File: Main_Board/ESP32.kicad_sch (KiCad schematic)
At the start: 24 parts, among them J1 RESET, J2 MAIN_UART, Q1 2N7002, U1 W25Q128JVS, U2 ESP32-S3-MINI-1U

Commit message: sch update
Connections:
- net CLK_SPI2: now also U2.17 (IO13); no longer U2.18 (IO14)
- net IO0 / MOSI: now also U2.18 (IO14); no longer U2.17 (IO13)
- net IO2 / WP: now also U2.19 (IO15); no longer U2.16 (IO12)
- net IO3 / HOLD: now also U2.16 (IO12); no longer U2.19 (IO15)
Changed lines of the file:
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@@
+	(wire
+		(pts
+			(xy 97.79 110.49) (xy 57.15 110.49)
+		)
+		(stroke
+			(width 0)
+			(type default)
+		)
+	)
+	(wire
+		(pts
+			(xy 104.14 107.95) (xy 104.14 110.49)
+		)
+		(stroke
+			(width 0)
+			(type default)
+		)
+	)
+	(wire
+		(pts
+			(xy 97.79 102.87) (xy 97.79 110.49)
+		)
+		(stroke
+			(width 0)
+			(type default)
+		)
+	)
 	(wire
 		(pts
@@
 	(wire
 		(pts
-			(xy 107.95 100.33) (xy 107.95 107.95)
+			(xy 107.95 100.33) (xy 107.95 105.41)
 		)
 		(stroke
@@
 	(wire
 		(pts
+			(xy 115.57 102.87) (xy 97.79 102.87)
+		)
+		(stroke
+			(width 0)
+			(type default)
+		)
+	)
+	(wire
+		(pts
 			(xy 36.83 36.83) (xy 36.83 55.88)
 		)
@@
 	(wire
 		(pts
-			(xy 115.57 105.41) (xy 92.71 105.41)
-		)
-		(stroke
-			(width 0)
-			(type default)
-		)
-	)
-	(wire
-		(pts
 			(xy 190.5 57.15) (xy 191.77 57.15)
 		)
@@
 	(wire
 		(pts
+			(xy 105.41 107.95) (xy 105.41 105.41)
+		)
+		(stroke
+			(width 0)
+			(type default)
+		)
+	)
+	(wire
+		(pts
 			(xy 104.14 67.31) (xy 115.57 67.31)
 		)
@@
 	(wire
 		(pts
+			(xy 105.41 105.41) (xy 92.71 105.41)
+		)
+		(stroke
+			(width 0)
+			(type default)
+		)
+	)
+	(wire
+		(pts
 			(xy 160.02 110.49) (xy 146.05 110.49)
 		)
@@
 	(wire
 		(pts
-			(xy 104.14 102.87) (xy 104.14 107.95)
+			(xy 104.14 110.49) (xy 115.57 110.49)
 		)
 		(stroke
@@
 	(wire
 		(pts
-			(xy 115.57 107.95) (xy 107.95 107.95)
+			(xy 115.57 105.41) (xy 107.95 105.41)
 		)
 		(stroke
@@
 	(wire
 		(pts
-			(xy 115.57 102.87) (xy 104.14 102.87)
-		)
-		(stroke
-			(width 0)
-			(type default)
-		)
-	)
-	(wire
-		(pts
 			(xy 21.59 60.96) (xy 25.4 60.96)
 		)
@@
 	(wire
 		(pts
+			(xy 115.57 107.95) (xy 105.41 107.95)
+		)
+		(stroke
+			(width 0)
+			(type default)
+		)
+	)
+	(wire
+		(pts
 			(xy 229.87 64.77) (xy 223.52 64.77)
 		)
@@
 		)
 		(stroke
-			(width 0)
-			(type default)
-		)
-	)
-	(wire
-		(pts
-			(xy 57.15 110.49) (xy 115.57 110.49)
-		)
-		(stroke

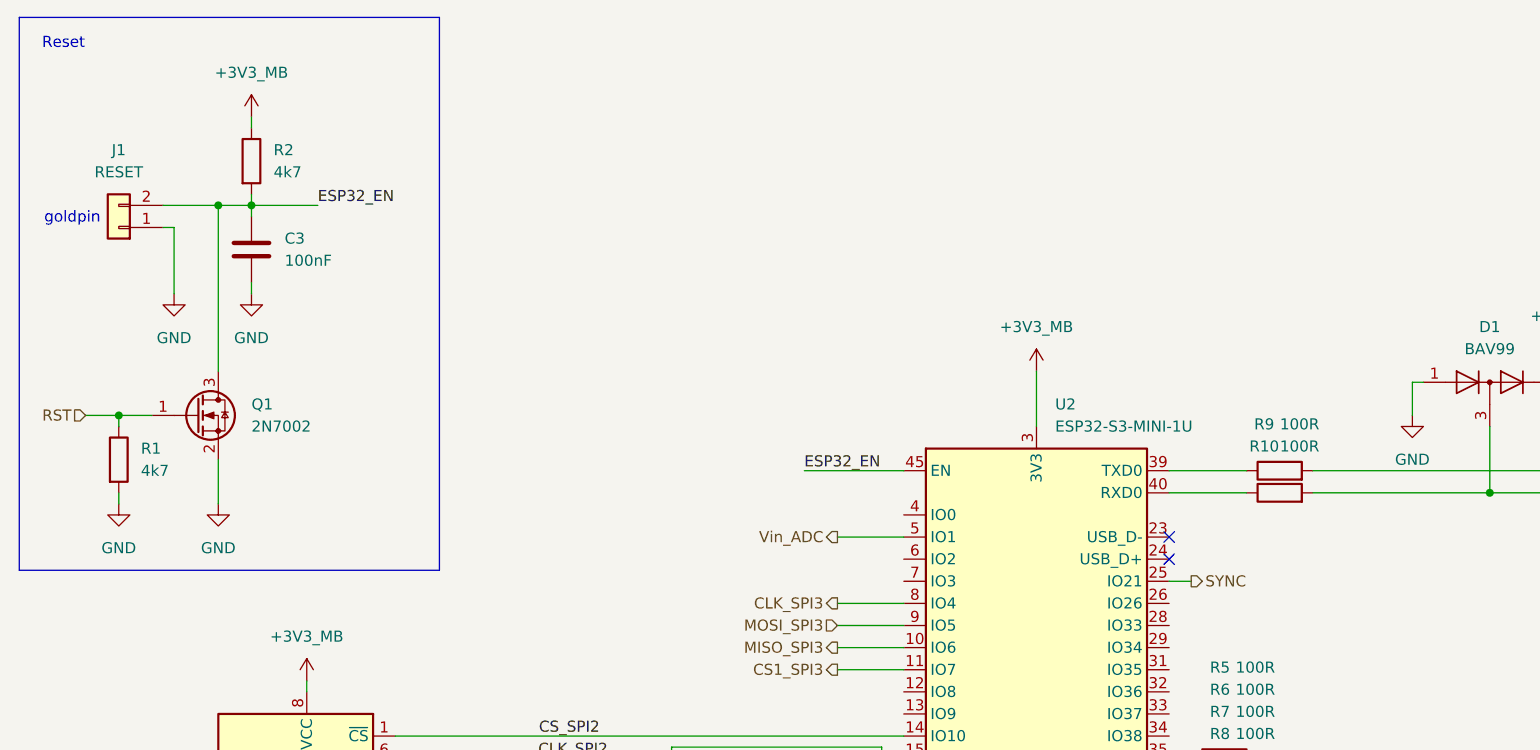
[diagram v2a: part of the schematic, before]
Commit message: Module bus fix
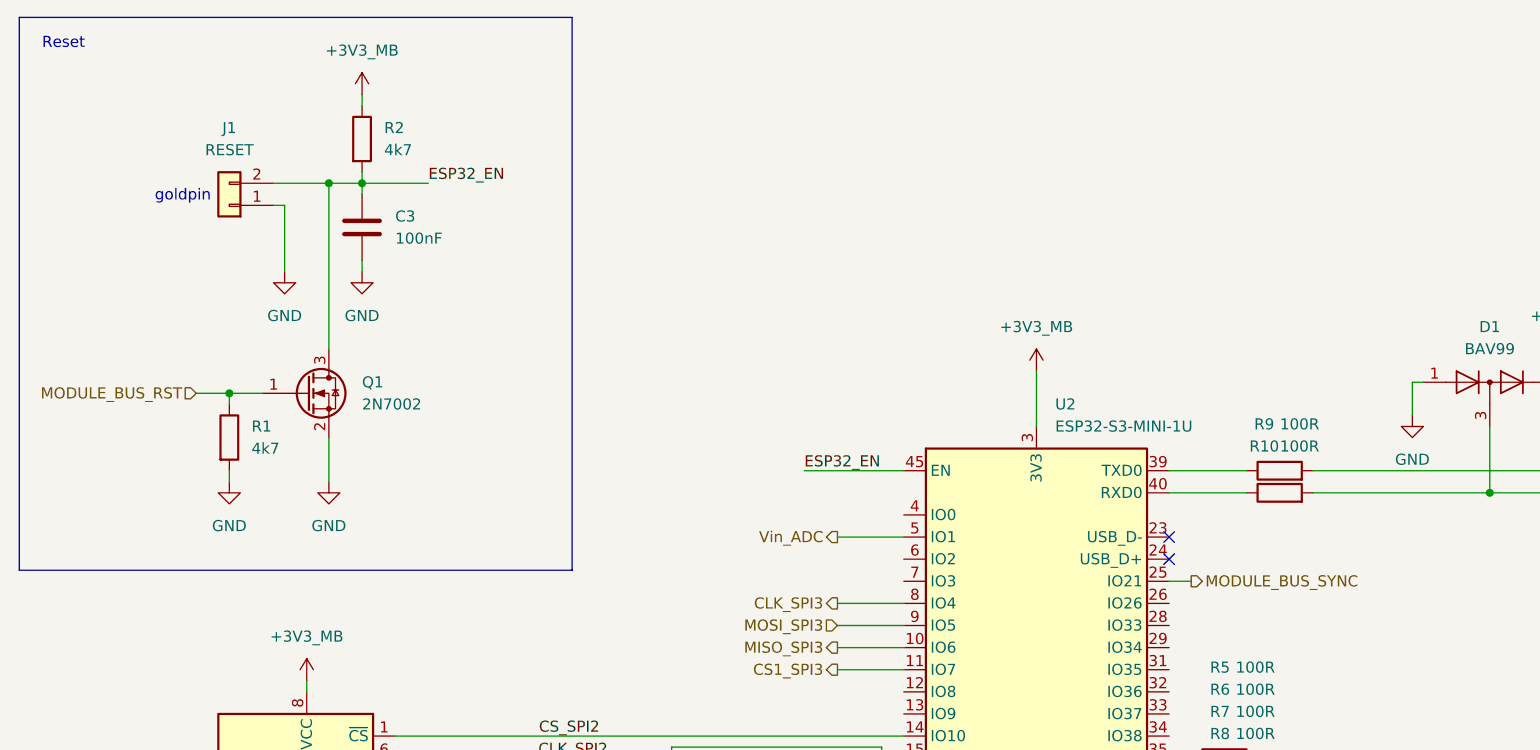
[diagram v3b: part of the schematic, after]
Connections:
- net RST renamed MODULE_BUS_RST
- net SYNC renamed MODULE_BUS_SYNC
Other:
- moved on the sheet: C3, J1, Q1, R1, R2

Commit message: Update main sheet for pyros
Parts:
- added R40, R41: 100R, Resistor_SMD:R_0603_1608Metric, symbol Device:R
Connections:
- net at U2.33 (IO37): now also R40.1
- net at U2.34 (IO38): now also R41.1
- net Piro1 renamed PYRO1
- net Piro2 renamed PYRO2
- new net PYRO1_CONTINUITY: R40.2
- new net PYRO2_CONTINUITY: R41.2

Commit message: Fix schematic readibility
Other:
- moved on the sheet: C3, D1, D2, J1, J2, Q1, R1, R10, R11, R2, R3, R4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

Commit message: Change connector footprints
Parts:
- J2: footprint Connector_PinHeader_2.54mm:PinHeader_1x04_P2.54mm_Horizontal -> Connector_PinHeader_2.54mm:PinHeader_1x04_P2.54mm_Vertical
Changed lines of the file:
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@@
 			)
 		)
-		(property "Footprint" "Connector_PinHeader_2.54mm:PinHeader_1x04_P2.54mm_Horizontal"
+		(property "Footprint" "Connector_PinHeader_2.54mm:PinHeader_1x04_P2.54mm_Vertical"
 			(at 252.73 99.06 0)
 			(hide yes)

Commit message: Remove buzzer circuitry
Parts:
- removed R6: 100R, Resistor_SMD:R_0603_1608Metric, symbol Device:R
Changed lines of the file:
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@@
-	(wire
-		(pts
-			(xy 156.21 134.62) (xy 158.75 134.62)
-		)
-		(stroke
-			(width 0)
-			(type default)
-		)
-	)
 	(wire
 		(pts
@@
 		(pts
 			(xy 245.11 96.52) (xy 247.65 96.52)
-		)
-		(stroke
-			(width 0)
-			(type default)
-		)
-	)
-	(wire
-		(pts
-			(xy 170.18 134.62) (xy 166.37 134.62)
 		)
 		(stroke
@@
 			)
 			(justify left bottom)
-		)
-	)
-	(hierarchical_label "BUZZER"
-		(shape output)
-		(at 170.18 134.62 0)
-		(effects
-			(font
-				(size 1.27 1.27)
-			)
-			(justify left)
 		)
 	)
@@
 					(unit 1)
 				)
-			)
-		)
-	)
-	(symbol
-		(lib_id "Device:R")
-		(at 162.56 134.62 90)
-		(unit 1)
-		(body_style 1)
-		(exclude_from_sim no)
-		(in_bom yes)
-		(on_board yes)
-		(in_pos_files yes)
-		(dnp no)
-		(property "Reference" "R6"
-			(at 181.61 134.62 90)
-			(show_name no)
-			(do_not_autoplace no)
-			(effects
-				(font
-					(size 1.27 1.27)
-				)
-			)
-		)
-		(property "Value" "100R"
-			(at 185.674 134.62 90)
-			(show_name no)
-			(do_not_autoplace no)
-			(effects
-				(font
-					(size 1.27 1.27)
-				)
-			)
-		)
-		(property "Footprint" "Resistor_SMD:R_0603_1608Metric"
-			(at 162.56 136.398 90)
-			(hide yes)
-			(show_name no)
-			(do_not_autoplace no)
-			(effects
-				(font
-					(size 1.27 1.27)
-				)
-			)
-		)
-		(property "Datasheet" ""
-			(at 162.56 134.62 0)
-			(hide yes)
-			(show_name no)
-			(do_not_autoplace no)
-			(effects
-				(font
-					(size 1.27 1.27)
-				)
-			)
-		)
-		(property "Description" "Resistor"
-			(at 162.56 134.62 0)
-			(hide yes)
-			(show_name no)
-			(do_not_autoplace no)
-			(effects
-				(font
-					(size 1.27 1.27)
-				)
-			)
-		)
-		(pin "1"
-		)
-		(pin "2"
-		)
-		(instances
-			(project "Main_Board"
-				(path "/7481738f-7c20-40bb-99b0-6ccd4168db33/cbc83c60-d43e-479b-a6b3-ba8e24d176e0"
-					(reference "R6")
-					(unit 1)
-				)

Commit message: layout update
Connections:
- net CLK_SPI3 is gone; now on an unnamed net: U2.8 (IO4)
- net CS1_SPI3 is gone; now on an unnamed net: U2.11 (IO7)
- net MISO_SPI3 is gone; now on an unnamed net: U2.10 (IO6)
- net MOSI_SPI3 is gone; now on an unnamed net: U2.9 (IO5)
- net at R41.1: no longer U2.34 (IO38)
- net at R40.1: no longer U2.33 (IO37)
- net at R7.1: no longer U2.37 (IO41)
- net at R8.1: no longer U2.38 (IO42)
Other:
- moved on the sheet: R40, R41, R7, R8
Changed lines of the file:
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@@
 	(wire
 		(pts
-			(xy 156.21 129.54) (xy 158.75 129.54)
-		)
-		(stroke
-			(width 0)
-			(type default)
-		)
-	)
-	(wire
-		(pts
 			(xy 233.68 96.52) (xy 233.68 86.36)
 		)
@@
 	(wire
 		(pts
-			(xy 170.18 129.54) (xy 166.37 129.54)
+			(xy 106.68 116.84) (xy 110.49 116.84)
 		)
 		(stroke
@@
 	(wire
 		(pts
-			(xy 170.18 127) (xy 166.37 127)
+			(xy 106.68 114.3) (xy 110.49 114.3)
 		)
 		(stroke
@@
 	(wire
 		(pts
-			(xy 170.18 139.7) (xy 166.37 139.7)
+			(xy 106.68 121.92) (xy 110.49 121.92)
 		)
 		(stroke
@@
 	(wire
 		(pts
-			(xy 170.18 137.16) (xy 166.37 137.16)
+			(xy 106.68 119.38) (xy 110.49 119.38)
 		)
 		(stroke
@@
 	(wire
 		(pts
-			(xy 156.21 127) (xy 158.75 127)
-		)
-		(stroke
-			(width 0)
-			(type default)
-		)
-	)
-	(wire
-		(pts
 			(xy 140.97 87.63) (xy 140.97 93.98)
 		)
@@
 		)
 	)
-	(hierarchical_label "CLK_SPI3"
-		(shape output)
-		(at 118.11 114.3 180)
-		(effects
-			(font
-				(size 1.27 1.27)
-			)
-			(justify right)
-		)
-	)
 	(hierarchical_label "5V_PG"
 		(shape output)
@@
 	(hierarchical_label "PYRO2_CONTINUITY"
 		(shape input)
-		(at 170.18 129.54 0)
-		(effects
-			(font
-				(size 1.27 1.27)
-			)
-			(justify left)
-		)
-	)
-	(hierarchical_label "MISO_SPI3"
-		(shape output)
-		(at 118.11 119.38 180)
+		(at 106.68 116.84 180)
 		(effects
 			(font
@@
 	(hierarchical_label "PYRO1_CONTINUITY"
 		(shape input)
-		(at 170.18 127 0)
+		(at 106.68 114.3 180)
 		(effects
 			(font
 				(size 1.27 1.27)
 			)
-			(justify left)
+			(justify right)
 		)
 	)
 	(hierarchical_label "PYRO1"
 		(shape output)
-		(at 170.18 137.16 0)
-		(effects
-			(font
-				(size 1.27 1.27)
-			)
-			(justify left)
-		)
-	)
-	(hierarchical_label "CS1_SPI3"
-		(shape output)
-		(at 118.11 121.92 180)
+		(at 106.68 119.38 180)
 		(effects
 			(font
@@
 	(hierarchical_label "PYRO2"
 		(shape output)
-		(at 170.18 139.7 0)
+		(at 106.68 121.92 180)
 		(effects
 			(font
 				(size 1.27 1.27)
 			)
-			(justify left)
+			(justify right)
 		)
 	)
@@
 		)
 	)
-	(hierarchical_label "MOSI_SPI3"
-		(shape input)
-		(at 118.11 116.84 180)
-		(effects
-			(font
-				(size 1.27 1.27)
-			)
-			(justify right)
-		)
-	)
 	(symbol
 		(lib_id "power:GND")
@@
 	(symbol
 		(lib_id "Device:R")
-		(at 162.56 129.54 90)
+		(at 114.3 116.84 270)
+		(mirror x)
 		(unit 1)
 		(body_style 1)
@@
 		(dnp no)
 		(property "Reference" "R41"
-			(at 192.278 129.54 90)
+			(at 84.582 116.84 90)
 			(show_name no)
 			(do_not_autoplace no)
@@
 		)
 		(property "Value" "100R"
-			(at 197.104 129.54 90)
+			(at 79.756 116.84 90)
 			(show_name no)
 			(do_not_autoplace no)
@@
 		)
 		(property "Footprint" "Resistor_SMD:R_0603_1608Metric"
-			(at 162.56 131.318 90)
+			(at 114.3 118.618 90)
 			(hide yes)
 			(show_name no)
@@
 		)
 		(property "Datasheet" ""
-			(at 162.56 129.54 0)
+			(at 114.3 116.84 0)
 			(hide yes)
 			(show_name no)
@@
 		)
 		(property "Description" "Resistor"
-			(at 162.56 129.54 0)
+			(at 114.3 116.84 0)
 			(hide yes)
 			(show_name no)
@@
 	(symbol
 		(lib_id "Device:R")
-		(at 162.56 127 90)
+		(at 114.3 114.3 270)
+		(mirror x)
 		(unit 1)
 		(body_style 1)
@@
 		(dnp no)
 		(property "Reference" "R40"
-			(at 192.278 127 90)
+			(at 84.582 114.3 90)
 			(show_name no)
 			(do_not_autoplace no)
@@
 		)
 		(property "Value" "100R"
-			(at 197.104 127 90)
+			(at 79.756 114.3 90)
 			(show_name no)
 			(do_not_autoplace no)
@@
 		)
 		(property "Footprint" "Resistor_SMD:R_0603_1608Metric"
-			(at 162.56 128.778 90)
+			(at 114.3 116.078 90)
 			(hide yes)
 			(show_name no)
@@
 		)
 		(property "Datasheet" ""
-			(at 162.56 127 0)
+			(at 114.3 114.3 0)
 			(hide yes)
 			(show_name no)
@@
 		)
 		(property "Description" "Resistor"
-			(at 162.56 127 0)
+			(at 114.3 114.3 0)
 			(hide yes)
 			(show_name no)
@@
 	(symbol
 		(lib_id "Device:R")
-		(at 162.56 137.16 90)
+		(at 114.3 119.38 270)
+		(mirror x)
 		(unit 1)
 		(body_style 1)
@@
 		(dnp no)
 		(property "Reference" "R7"
-			(at 181.61 137.16 90)
+			(at 95.25 119.38 90)
 			(show_name no)
 			(do_not_autoplace no)
@@
 		)
 		(property "Value" "100R"
-			(at 185.674 137.16 90)
+			(at 91.186 119.38 90)
 			(show_name no)
 			(do_not_autoplace no)
@@
 		)
 		(property "Footprint" "Resistor_SMD:R_0603_1608Metric"
-			(at 162.56 138.938 90)
+			(at 114.3 121.158 90)
 			(hide yes)
 			(show_name no)
@@
 		)
 		(property "Datasheet" ""
-			(at 162.56 137.16 0)
+			(at 114.3 119.38 0)
 			(hide yes)
 			(show_name no)
@@
 		)
 		(property "Description" "Resistor"
-			(at 162.56 137.16 0)
+			(at 114.3 119.38 0)
 			(hide yes)
 			(show_name no)
@@
 	(symbol
 		(lib_id "Device:R")
-		(at 162.56 139.7 90)
+		(at 114.3 121.92 270)
+		(mirror x)
 		(unit 1)
 		(body_style 1)
@@
 		(dnp no)
 		(property "Reference" "R8"
-			(at 181.61 139.7 90)
+			(at 95.25 121.92 90)
 			(show_name no)
 			(do_not_autoplace no)
@@
 		)
 		(property "Value" "100R"
-			(at 185.674 139.7 90)
+			(at 91.186 121.92 90)
 			(show_name no)
 			(do_not_autoplace no)
@@
 		)
 		(property "Footprint" "Resistor_SMD:R_0603_1608Metric"
-			(at 162.56 141.478 90)
+			(at 114.3 123.698 90)
 			(hide yes)
 			(show_name no)
@@
 		)
 		(property "Datasheet" ""
-			(at 162.56 139.7 0)
+			(at 114.3 121.92 0)
 			(hide yes)
 			(show_name no)
@@
 		)
 		(property "Description" "Resistor"
-			(at 162.56 139.7 0)
+			(at 114.3 121.92 0)
 			(hide yes)
 			(show_name no)
